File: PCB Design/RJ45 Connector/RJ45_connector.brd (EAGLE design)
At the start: 27.6 x 25.4 mm, 3 parts, among them X1 RJ45-8L-B

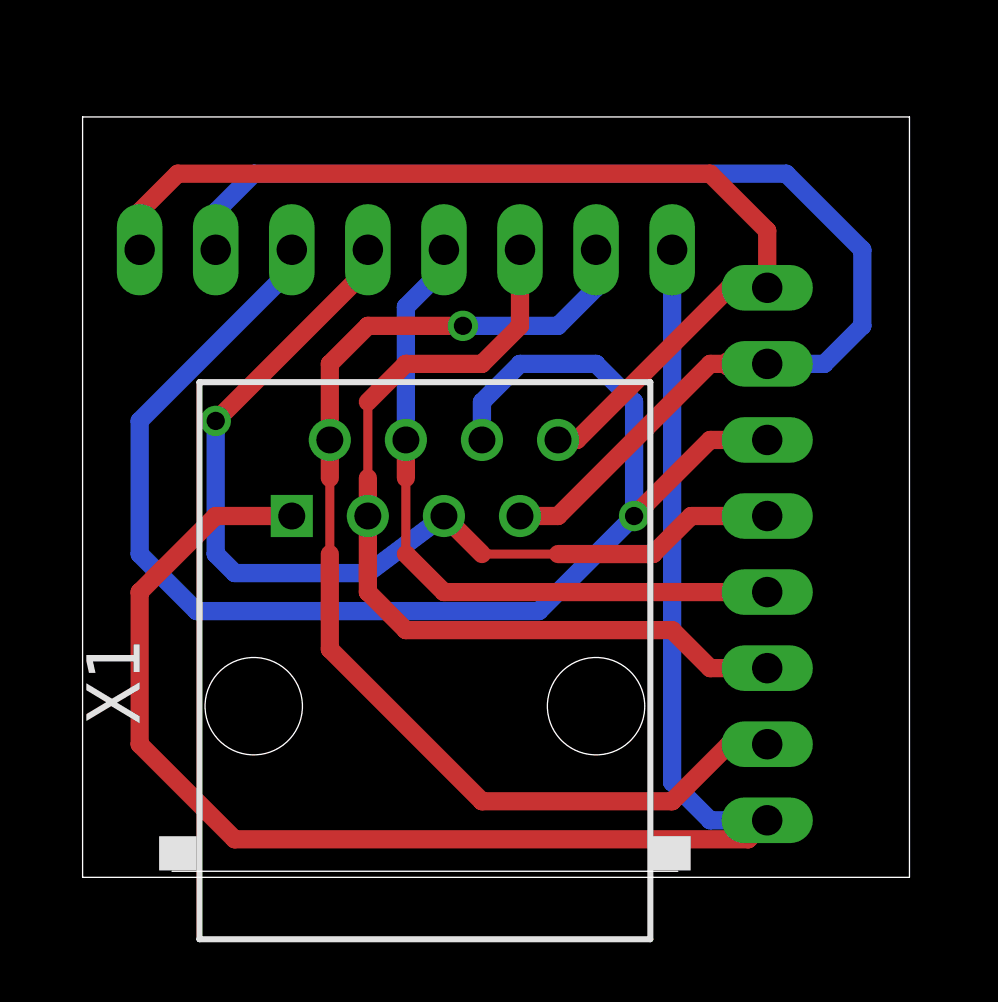
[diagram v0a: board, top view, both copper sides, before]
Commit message: Changed location of the header to make it much easier to router
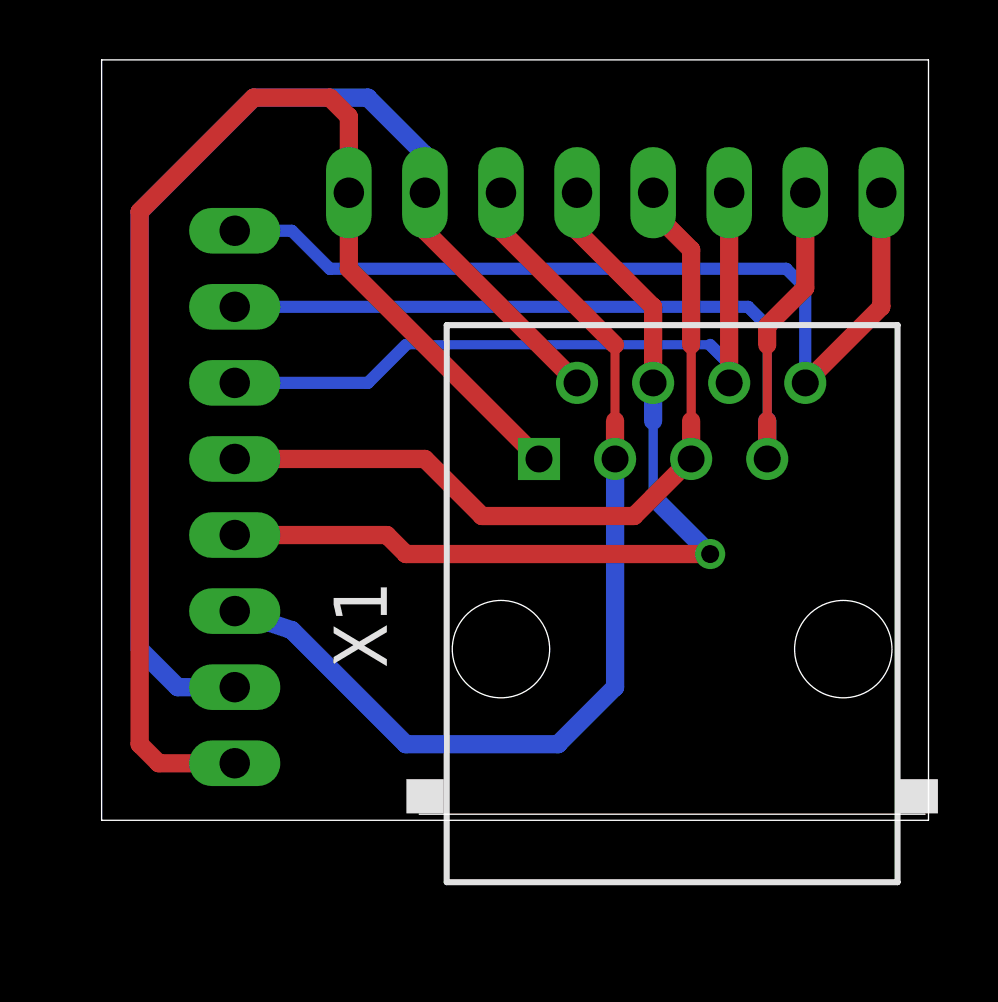
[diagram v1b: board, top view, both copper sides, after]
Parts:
- moved JP1 18.2 mm to (17.1, 24.8), turned to 0 degrees
- moved JP2 15.4 mm to (0.64, 10.8), turned to 270 degrees
- moved X1 8.47 mm to (19.1, 5.71)
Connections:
- net N$1: now also JP1.1, JP2.1; no longer JP1.8, JP2.8
- net N$2: now also JP1.2, JP2.2; no longer JP1.7, JP2.7
- net N$3: now also JP1.3, JP2.3; no longer JP1.6, JP2.6
- net N$4: now also JP1.4, JP2.4; no longer JP1.5, JP2.5
- net N$5: now also JP1.5, JP2.5; no longer JP1.4, JP2.4
- net N$6: now also JP1.6, JP2.6; no longer JP1.3, JP2.3
- net N$7: now also JP1.7, JP2.7; no longer JP1.2, JP2.2
- net N$8: now also JP1.8, JP2.8; no longer JP1.1, JP2.1
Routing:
- net N$3: track 47.6 -> 24.3 mm, vias 1 -> 0
- net N$8: track 55.2 -> 44.1 mm
- net N$2: track 42.3 -> 31.9 mm
- net N$4: track 33.9 -> 26.2 mm, vias 1 -> 0
- net N$5: track 23.3 -> 30.0 mm, vias 0 -> 1
- net N$1: track 34.5 -> 30.4 mm
- net N$6: track 30.7 -> 33.3 mm
- net N$7: track 38.2 -> 39.9 mm, vias 1 -> 0
